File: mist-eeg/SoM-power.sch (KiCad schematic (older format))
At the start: 14 parts, among them U9 TPS63070

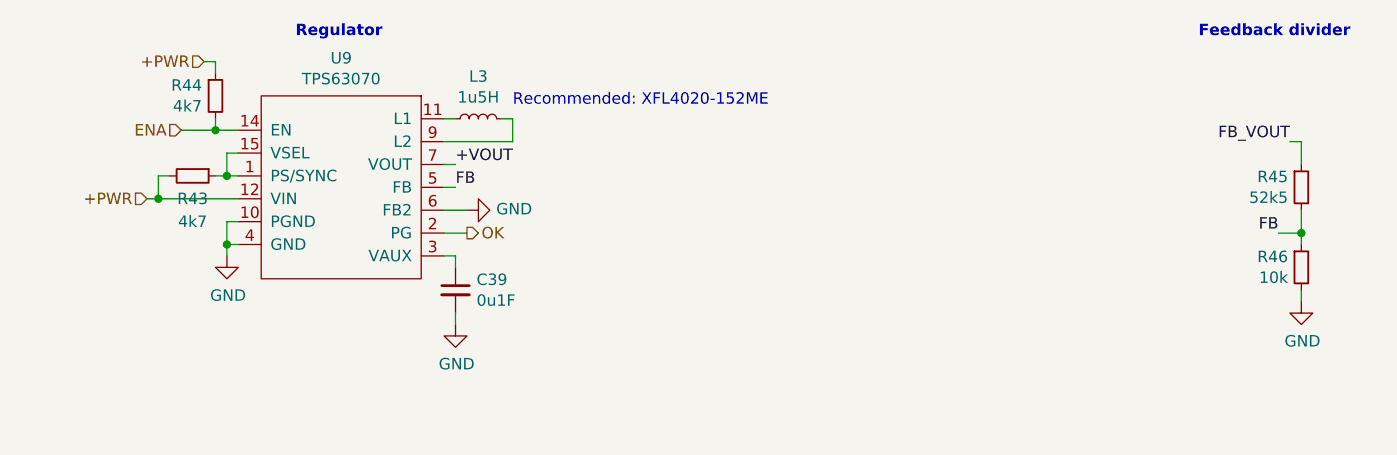
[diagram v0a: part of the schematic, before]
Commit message: Finish schematic and create interface specifications
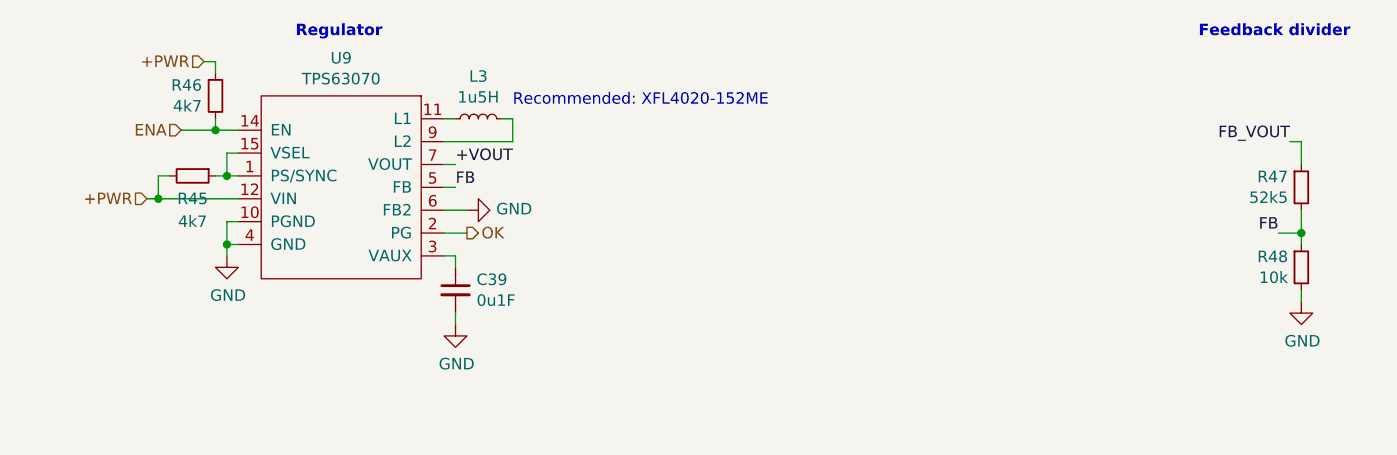
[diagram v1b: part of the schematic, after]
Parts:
- renumbered R43 to R45, R44 to R46, R45 to R47, R46 to R48
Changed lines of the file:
@@
 P 4200 2500
 AR Path="/609A79EB/60F89803/6137E5B8" Ref="R?"  Part="1"
-AR Path="/609A79EB/61372D3E/6137E5B8" Ref="R43"  Part="1"
-F 0 "R43" V 4300 2500 50  0000 C CNN
+AR Path="/609A79EB/61372D3E/6137E5B8" Ref="R45"  Part="1"
+F 0 "R45" V 4300 2500 50  0000 C CNN
 F 1 "4k7" V 4400 2500 50  0000 C CNN
 F 2 "Resistor_SMD:R_0201_0603Metric" H 4200 2500 50  0001 C CNN
@@
 P 9050 2550
 AR Path="/609A79EB/60F89803/6137E5FA" Ref="R?"  Part="1"
-AR Path="/609A79EB/61372D3E/6137E5FA" Ref="R45"  Part="1"
-F 0 "R45" H 8992 2596 50  0000 R CNN
+AR Path="/609A79EB/61372D3E/6137E5FA" Ref="R47"  Part="1"
+F 0 "R47" H 8992 2596 50  0000 R CNN
 F 1 "52k5" H 8992 2505 50  0000 R CNN
 F 2 "Resistor_SMD:R_0603_1608Metric" H 9050 2550 50  0001 C CNN
@@
 P 9050 2900
 AR Path="/609A79EB/60F89803/6137E600" Ref="R?"  Part="1"
-AR Path="/609A79EB/61372D3E/6137E600" Ref="R46"  Part="1"
-F 0 "R46" H 8992 2946 50  0000 R CNN
+AR Path="/609A79EB/61372D3E/6137E600" Ref="R48"  Part="1"
+F 0 "R48" H 8992 2946 50  0000 R CNN
 F 1 "10k" H 8992 2855 50  0000 R CNN
 F 2 "Resistor_SMD:R_0603_1608Metric" H 9050 2900 50  0001 C CNN
@@
 P 4300 2150
 AR Path="/609A79EB/60F89803/6137E61B" Ref="R?"  Part="1"
-AR Path="/609A79EB/61372D3E/6137E61B" Ref="R44"  Part="1"
-F 0 "R44" H 4241 2196 50  0000 R CNN
+AR Path="/609A79EB/61372D3E/6137E61B" Ref="R46"  Part="1"
+F 0 "R46" H 4241 2196 50  0000 R CNN
 F 1 "4k7" H 4241 2105 50  0000 R CNN
 F 2 "Resistor_SMD:R_0201_0603Metric" H 4300 2150 50  0001 C CNN
@@
 P 2850 4900
 AR Path="/609A79EB/60F89803/6137E649" Ref="#PWR?"  Part="1"
-AR Path="/609A79EB/61372D3E/6137E649" Ref="#PWR059"  Part="1"
-F 0 "#PWR059" H 2850 4650 50  0001 C CNN
+AR Path="/609A79EB/61372D3E/6137E649" Ref="#PWR060"  Part="1"
+F 0 "#PWR060" H 2850 4650 50  0001 C CNN
 F 1 "GND" V 2855 4772 50  0000 R CNN
 F 2 "" H 2850 4900 50  0001 C CNN
@@
 P 6650 5000
 AR Path="/609A79EB/60F89803/6137E64F" Ref="#PWR?"  Part="1"
-AR Path="/609A79EB/61372D3E/6137E64F" Ref="#PWR063"  Part="1"
-F 0 "#PWR063" H 6650 4750 50  0001 C CNN
+AR Path="/609A79EB/61372D3E/6137E64F" Ref="#PWR064"  Part="1"
+F 0 "#PWR064" H 6650 4750 50  0001 C CNN
 F 1 "GND" H 6655 4827 50  0000 C CNN
 F 2 "" H 6650 5000 50  0001 C CNN
@@
 P 4350 2850
 AR Path="/609A79EB/60F89803/6137E655" Ref="#PWR?"  Part="1"
-AR Path="/609A79EB/61372D3E/6137E655" Ref="#PWR060"  Part="1"
-F 0 "#PWR060" H 4350 2600 50  0001 C CNN
+AR Path="/609A79EB/61372D3E/6137E655" Ref="#PWR061"  Part="1"
+F 0 "#PWR061" H 4350 2600 50  0001 C CNN
 F 1 "GND" H 4355 2677 50  0000 C CNN
 F 2 "" H 4350 2850 50  0001 C CNN
@@
 P 5350 3150
 AR Path="/609A79EB/60F89803/6137E65B" Ref="#PWR?"  Part="1"
-AR Path="/609A79EB/61372D3E/6137E65B" Ref="#PWR061"  Part="1"
-F 0 "#PWR061" H 5350 2900 50  0001 C CNN
+AR Path="/609A79EB/61372D3E/6137E65B" Ref="#PWR062"  Part="1"
+F 0 "#PWR062" H 5350 2900 50  0001 C CNN
 F 1 "GND" H 5355 2977 50  0000 C CNN
 F 2 "" H 5350 3150 50  0001 C CNN
@@
 P 5400 2650
 AR Path="/609A79EB/60F89803/6137E661" Ref="#PWR?"  Part="1"
-AR Path="/609A79EB/61372D3E/6137E661" Ref="#PWR062"  Part="1"
-F 0 "#PWR062" H 5400 2400 50  0001 C CNN
+AR Path="/609A79EB/61372D3E/6137E661" Ref="#PWR063"  Part="1"
+F 0 "#PWR063" H 5400 2400 50  0001 C CNN
 F 1 "GND" V 5405 2522 50  0000 R CNN
 F 2 "" H 5400 2650 50  0001 C CNN
@@
 P 9050 3050
 AR Path="/609A79EB/60F89803/6137E667" Ref="#PWR?"  Part="1"
-AR Path="/609A79EB/61372D3E/6137E667" Ref="#PWR064"  Part="1"
-F 0 "#PWR064" H 9050 2800 50  0001 C CNN
+AR Path="/609A79EB/61372D3E/6137E667" Ref="#PWR065"  Part="1"
+F 0 "#PWR065" H 9050 2800 50  0001 C CNN
 F 1 "GND" H 9055 2877 50  0000 C CNN
 F 2 "" H 9050 3050 50  0001 C CNN

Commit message: Place components
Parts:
- removed C43: 22uF, Capacitor_SMD:C_0603_1608Metric, symbol Device:C_Small
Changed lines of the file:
@@
 Wire Wire Line
 	6950 4450 6950 4600
-Wire Wire Line
-	7100 4450 6950 4450
-Wire Wire Line
-	7100 4450 7150 4450
-Connection ~ 7100 4450
-Wire Wire Line
-	7100 4450 7100 4600
-$Comp
-L Device:C_Small C?
-U 1 1 6137E636
-P 7100 4700
-AR Path="/609A79EB/60F89803/6137E636" Ref="C?"  Part="1"
-AR Path="/609A79EB/61372D3E/6137E636" Ref="C43"  Part="1"
-F 0 "C43" V 7050 4750 50  0000 L CNN
-F 1 "22uF" H 7100 4600 50  0000 C CNN
-F 2 "Capacitor_SMD:C_0603_1608Metric" H 7100 4700 50  0001 C CNN
-F 3 "~" H 7100 4700 50  0001 C CNN
-	1    7100 4700
-	1    0    0    -1
-$EndComp
 $Comp
 L Device:C_Small C?
@@
 $EndComp
 Wire Wire Line
-	7100 4800 7100 4950
-Wire Wire Line
 	6950 4800 6950 4950
-Wire Wire Line
-	6950 4950 7100 4950
-Connection ~ 6950 4950
 Connection ~ 6800 4950
 Wire Wire Line
@@
 	1    0    0    -1
 $EndComp
+Wire Wire Line
+	6950 4450 7150 4450
 $EndSCHEMATC

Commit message: Advance routing
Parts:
- removed R46: 4k7, Resistor_SMD:R_0201_0603Metric, symbol Device:R_Small
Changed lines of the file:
@@
 $Descr A4 11693 8268
 encoding utf-8
-Sheet 7 12
+Sheet 6 11
 Title ""
 Date ""
@@
 Regulator
 $Comp
-L Device:R_Small R?
-U 1 1 6137E61B
-P 4300 2150
-AR Path="/609A79EB/60F89803/6137E61B" Ref="R?"  Part="1"
-AR Path="/609A79EB/61372D3E/6137E61B" Ref="R46"  Part="1"
-F 0 "R46" H 4241 2196 50  0000 R CNN
-F 1 "4k7" H 4241 2105 50  0000 R CNN
-F 2 "Resistor_SMD:R_0201_0603Metric" H 4300 2150 50  0001 C CNN
-F 3 "~" H 4300 2150 50  0001 C CNN
-	1    4300 2150
-	1    0    0    -1
-$EndComp
-Wire Wire Line
-	4300 2250 4300 2300
-Wire Wire Line
-	4300 2300 4400 2300
-Wire Wire Line
-	4300 2300 4150 2300
-Connection ~ 4300 2300
-Text HLabel 4250 2000 0    50   Input ~ 0
-+PWR
-Wire Wire Line
-	4250 2000 4300 2000
-Wire Wire Line
-	4300 2000 4300 2050
-$Comp
 L Device:C_Small C?
 U 1 1 6137E628
@@
 Wire Wire Line
 	6950 4450 7150 4450
+Wire Wire Line
+	4150 2300 4400 2300
 $EndSCHEMATC

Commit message: Validation & fabrication layer
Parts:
- R47: value 52k5 -> 52k3
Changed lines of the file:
@@
 Wire Wire Line
 	5400 2750 5300 2750
-Text HLabel 4150 2300 0    50   Input ~ 0
+Text HLabel 4350 2300 0    50   Input ~ 0
 ENA
 $Comp
@@
 AR Path="/609A79EB/61372D3E/6137E5FA" Ref="R47"  Part="1"
 F 0 "R47" H 8992 2596 50  0000 R CNN
-F 1 "52k5" H 8992 2505 50  0000 R CNN
+F 1 "52k3" H 8992 2505 50  0000 R CNN
 F 2 "Resistor_SMD:R_0603_1608Metric" H 9050 2550 50  0001 C CNN
 F 3 "~" H 9050 2550 50  0001 C CNN
@@
 	6950 4450 7150 4450
 Wire Wire Line
-	4150 2300 4400 2300
+	4350 2300 4400 2300
 $EndSCHEMATC

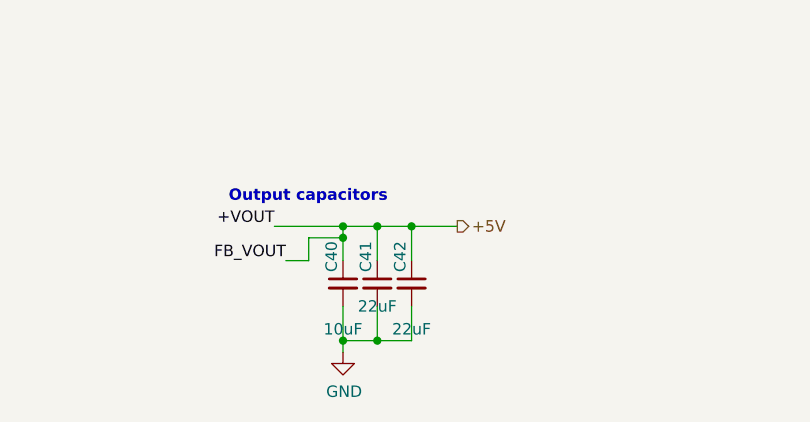
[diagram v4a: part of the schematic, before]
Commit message: Update footprints based upon piece availability & generate manufacturing files
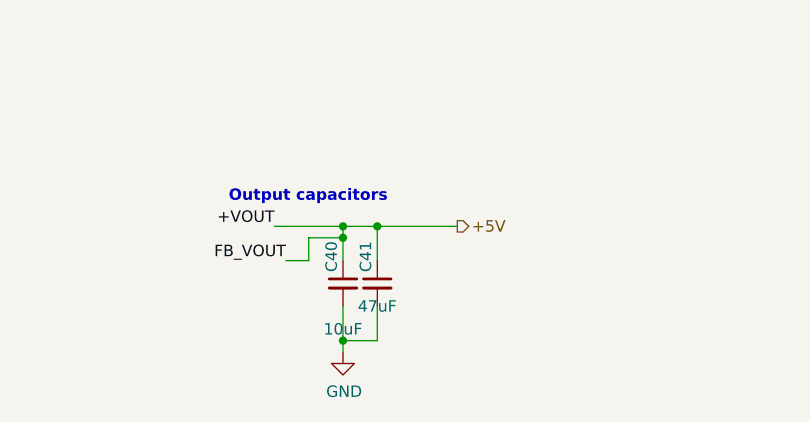
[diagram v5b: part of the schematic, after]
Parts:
- removed C42: 22uF, Capacitor_SMD:C_0603_1608Metric, symbol Device:C_Small
- C41: value 22uF -> 47uF; footprint Capacitor_SMD:C_0603_1608Metric -> Capacitor_SMD:C_1210_3225Metric
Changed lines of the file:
@@
 AR Path="/609A79EB/61372D3E/6137E628" Ref="C41"  Part="1"
 F 0 "C41" V 6750 4750 50  0000 L CNN
-F 1 "22uF" H 6800 4600 50  0000 C CNN
-F 2 "Capacitor_SMD:C_0603_1608Metric" H 6800 4700 50  0001 C CNN
+F 1 "47uF" H 6800 4600 50  0000 C CNN
+F 2 "Capacitor_SMD:C_1210_3225Metric" H 6800 4700 50  0001 C CNN
 F 3 "~" H 6800 4700 50  0001 C CNN
 	1    6800 4700
@@
 $EndComp
 Connection ~ 6800 4450
-Wire Wire Line
-	6950 4450 6800 4450
-Connection ~ 6950 4450
-Wire Wire Line
-	6950 4450 6950 4600
-$Comp
-L Device:C_Small C?
-U 1 1 6137E63C
-P 6950 4700
-AR Path="/609A79EB/60F89803/6137E63C" Ref="C?"  Part="1"
-AR Path="/609A79EB/61372D3E/6137E63C" Ref="C42"  Part="1"
-F 0 "C42" V 6900 4750 50  0000 L CNN
-F 1 "22uF" H 6950 4500 50  0000 C CNN
-F 2 "Capacitor_SMD:C_0603_1608Metric" H 6950 4700 50  0001 C CNN
-F 3 "~" H 6950 4700 50  0001 C CNN
-	1    6950 4700
-	1    0    0    -1
-$EndComp
-Wire Wire Line
-	6950 4800 6950 4950
-Connection ~ 6800 4950
-Wire Wire Line
-	6800 4950 6950 4950
 Text Notes 5600 2200 0    50   ~ 0
 Recommended: XFL4020-152ME
@@
 $EndComp
 Wire Wire Line
-	6950 4450 7150 4450
+	4350 2300 4400 2300
 Wire Wire Line
-	4350 2300 4400 2300
+	6800 4450 7150 4450
 $EndSCHEMATC

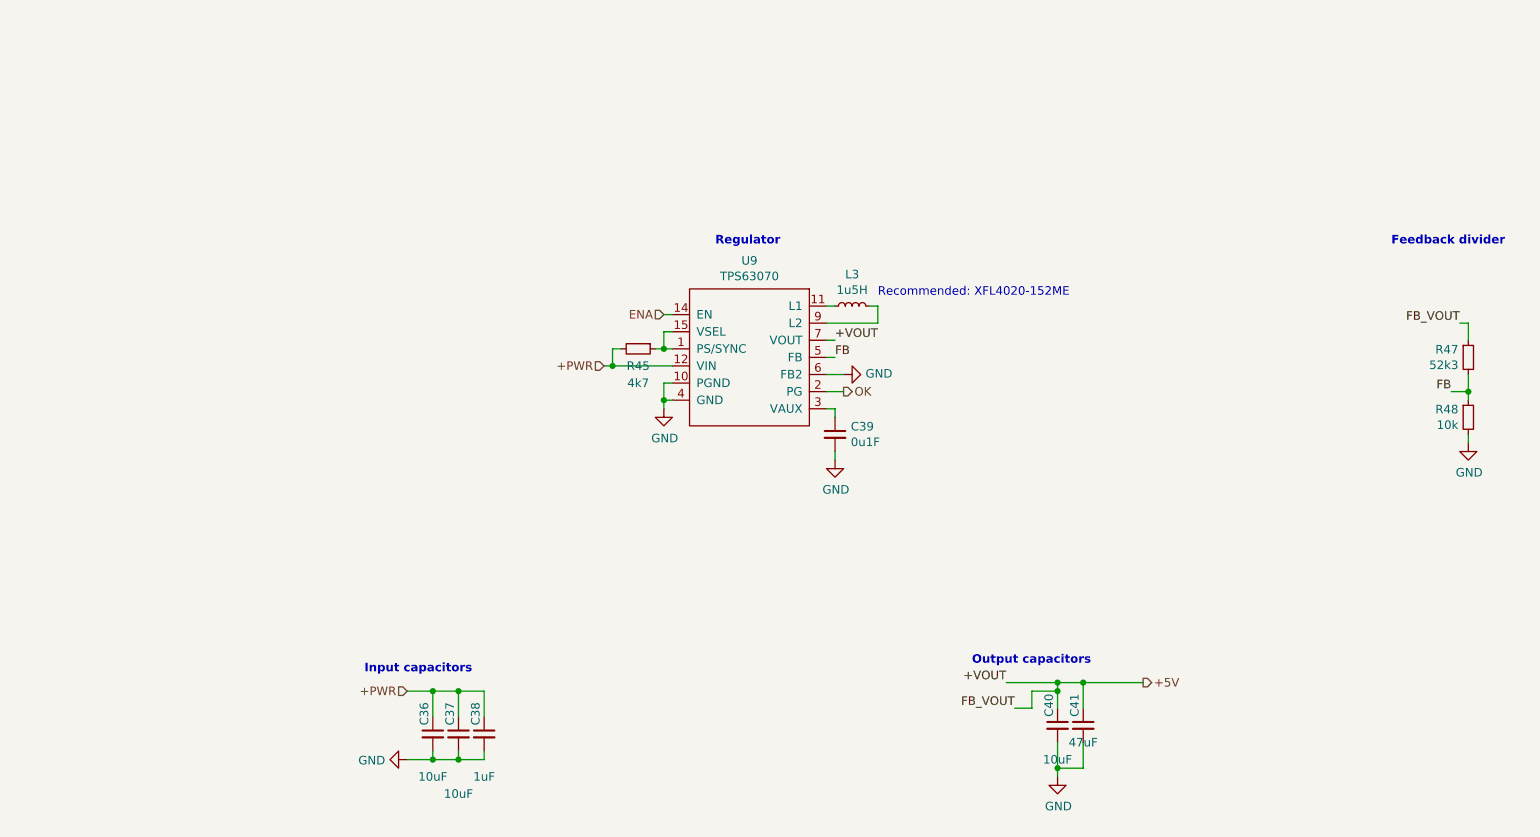
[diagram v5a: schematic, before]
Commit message: Change buckboost regulator used
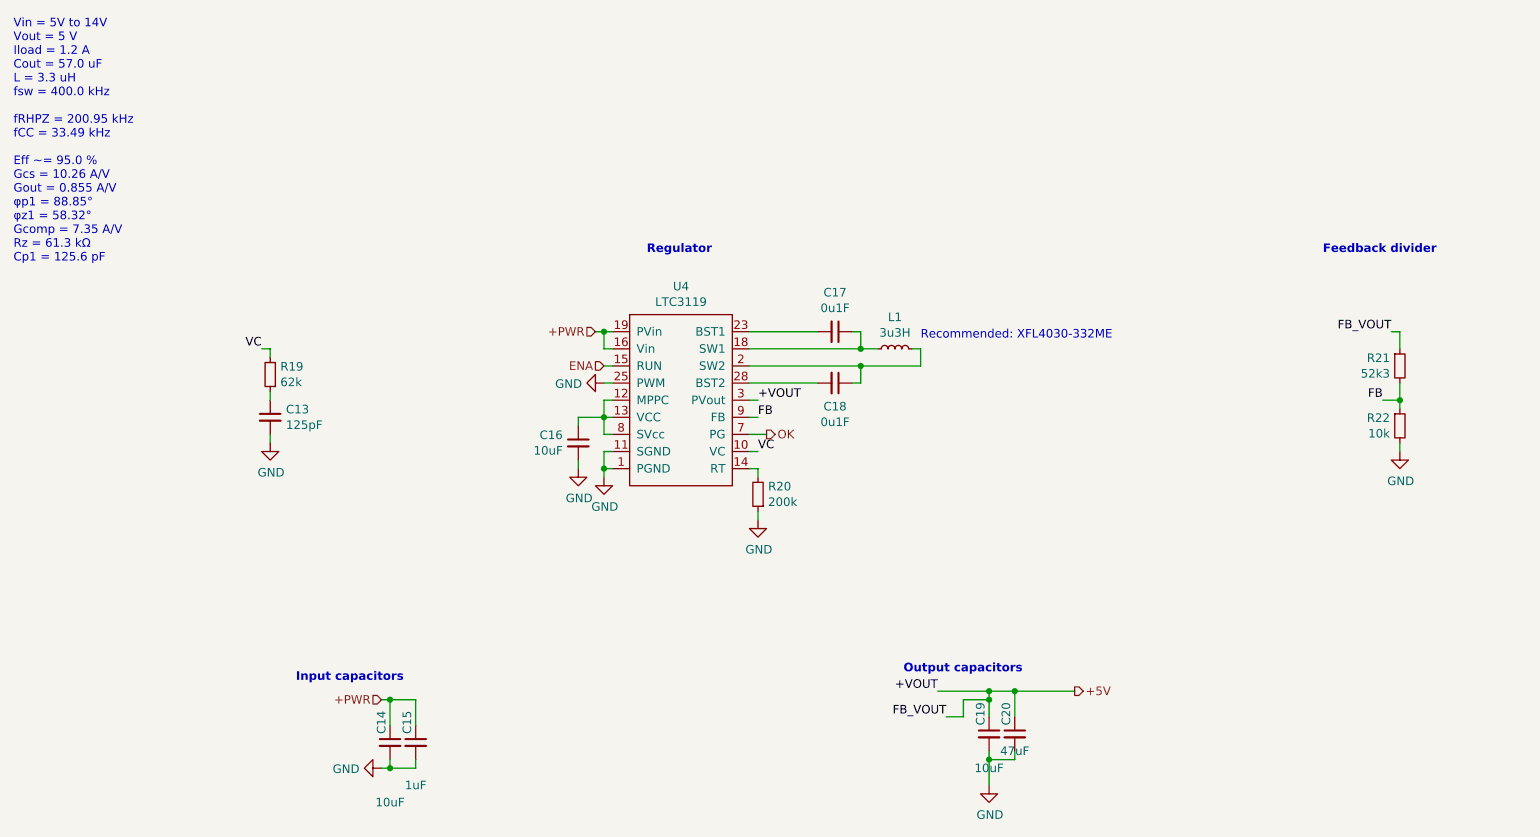
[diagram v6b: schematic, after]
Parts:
- removed C36: 10uF, Capacitor_SMD:C_0603_1608Metric, symbol Device:C_Small
- removed C39: 0u1F, Capacitor_SMD:C_0201_0603Metric, symbol Device:C_Small
- removed L3: 1u5H, Inductor_SMD:L_Coilcraft_XxL4040, symbol Device:L_Small
- removed R45: 4k7, Resistor_SMD:R_0201_0603Metric, symbol Device:R_Small
- removed U9: TPS63070, mist-eeg:TPS630702RNMR, symbol components:TPS63070
- added C13: 125pF, Capacitor_SMD:C_0201_0603Metric, symbol Device:C_Small
- added C16: 10uF, Capacitor_SMD:C_0603_1608Metric, symbol Device:C_Small
- added C17, C18: 0u1F, Capacitor_SMD:C_0201_0603Metric, symbol Device:C_Small
- added L1: 3u3H, Inductor_SMD:L_Coilcraft_XxL4040, symbol Device:L_Small
- added R19: 62k, Resistor_SMD:R_0201_0603Metric, symbol Device:R_Small
- added R20: 200k, Resistor_SMD:R_0201_0603Metric, symbol Device:R_Small
- added U4: LTC3119, Package_DFN_QFN:QFN-28-1EP_4x5mm_P0.5mm_EP2.65x3.65mm, symbol components:LTC3119
- renumbered C37 to C14, C38 to C15, C40 to C19, C41 to C20, R47 to R21, R48 to R22
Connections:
- net +5V: now also U4.3 (PVout), U4.4 (PVout)
- net +PWR: now also U4.16 (Vin), U4.19 (PVin), U4.20 (PVin)
- net ENA: now also U4.15 (RUN)
- net FB: now also U4.9 (FB)
- net GND: now also C13.2, C16.2, R20.1, U4.1 (PGND), U4.11 (SGND), U4.17 (PGND), U4.22 (PGND), U4.25 (PWM), U4.29 (PGND), U4.6 (PGND)
- net OK: now also U4.7 (PG)
- new net: C18.1, L1.2, U4.2 (SW2), U4.5 (SW2)
- new net: C18.2, U4.28 (BST2)
- new net: C17.1, L1.1, U4.18 (SW1), U4.21 (SW1)
- new net: C17.2, U4.23 (BST1)
- new net: C16.1, U4.12 (MPPC), U4.13 (VCC), U4.8 (SVcc)
- new net: R20.2, U4.14 (RT)
- new net: C13.1, R19.1
- new net VC: R19.2, U4.10 (VC)
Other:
- note added: "Recommended: XFL4030-332ME"
- note added: "Vin = 5V to 14V\nVout = 5 V\nIload = 1.2 A\nCout = 57.0 uF\nL = 3.3 uH\nfsw = 400.0 kHz\n\nfRHPZ = 200.95 kHz\nfCC = 33.49 kHz\n\nEff ~~= 95.0 %\nGcs = 10.26 A/V\nGout = 0.855 A/V\nφp1 = 88.85°\nφz1 = 58.32°\nGcomp = 7.35 A/V\nRz = 61.3 kΩ\nCp1 = 125.6 pF"
- note removed: "Recommended: XFL4020-152ME"
- moved on the sheet: C14, C15, C19, C20, R21, R22
